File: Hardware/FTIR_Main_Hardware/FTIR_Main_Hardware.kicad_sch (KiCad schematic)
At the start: 64 parts, among them J1 RJ45_LED_Shielded, Q1 IRF7606PBF, Q2 BSS138, Q3 IRF7606PBF, Q4 IRF7606PBF, Q5 BSS138, Q6 BSS138, U1 MCP6L01x-xOT, U3 OKI, U5 MCP6L01x-xOT, U6 Teensy4.1_DEV-16771, U7 OKI

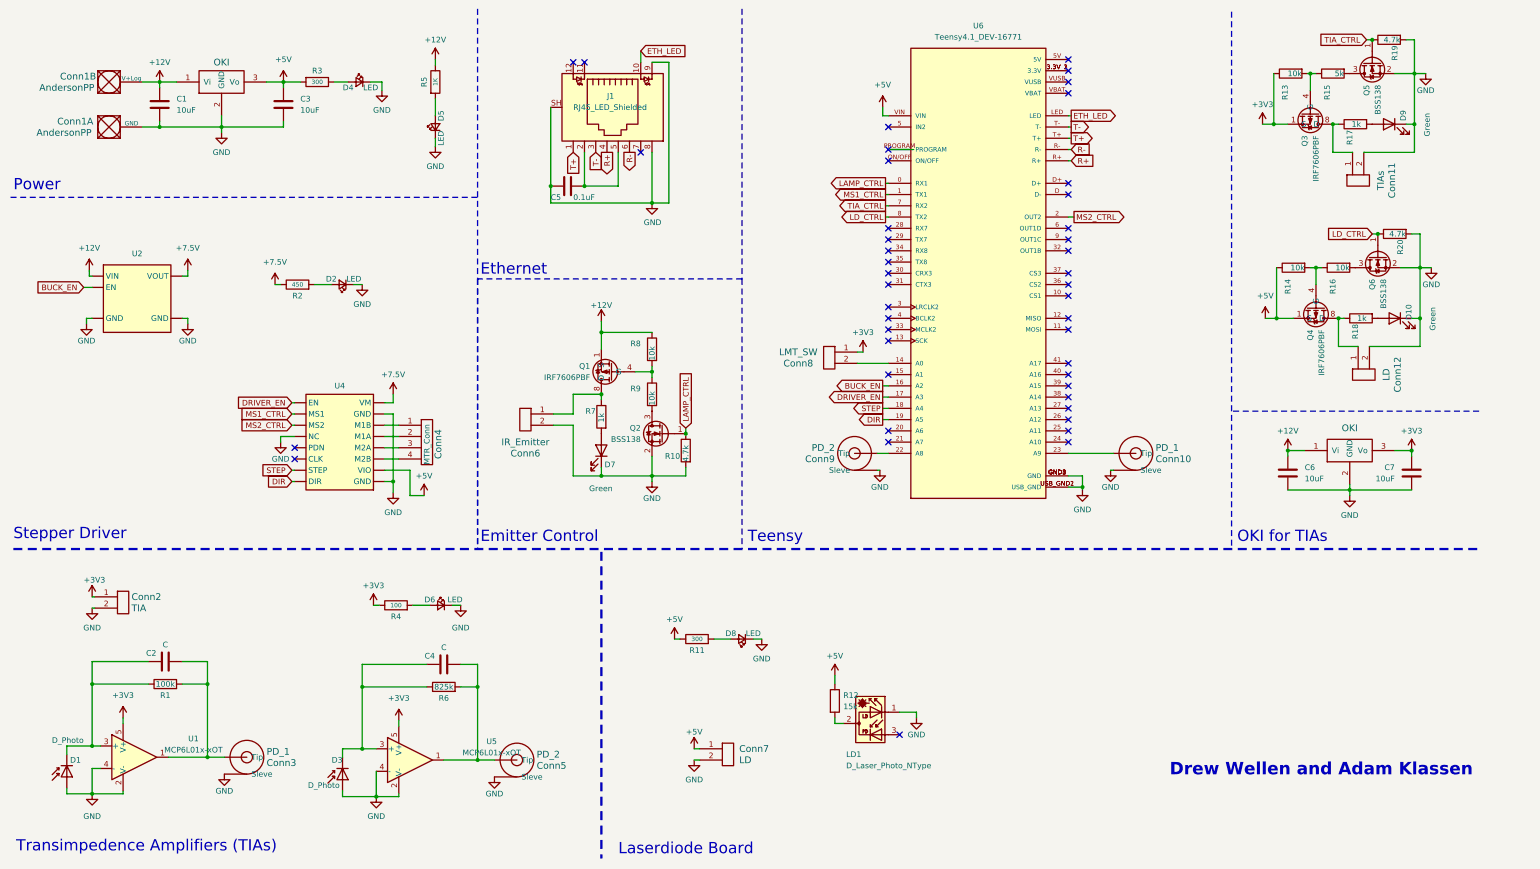
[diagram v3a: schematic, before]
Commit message: changed resistor values
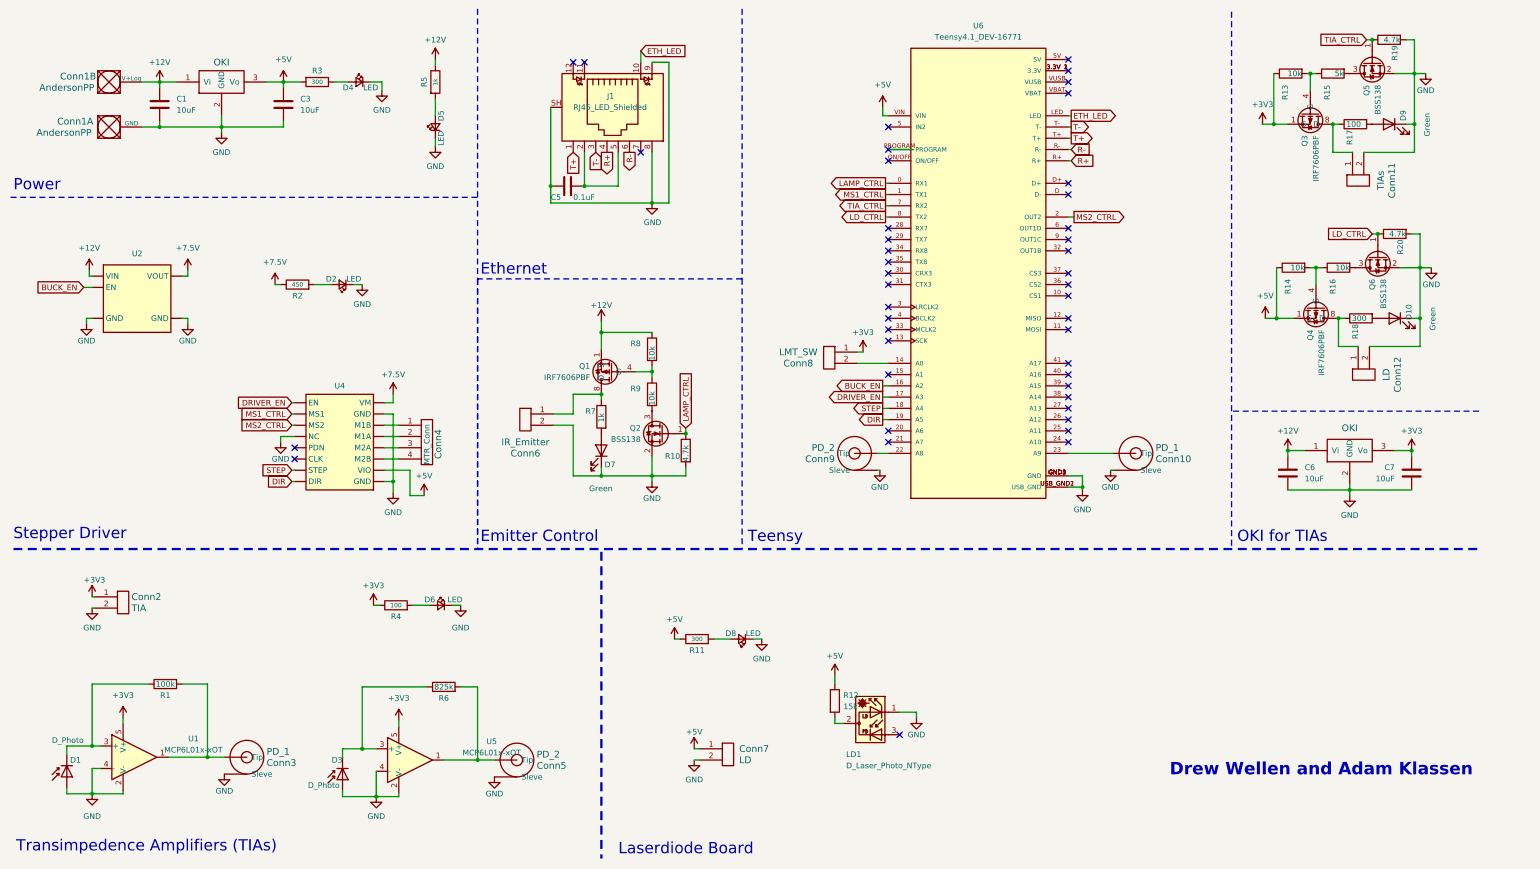
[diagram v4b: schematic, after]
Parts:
- removed C2, C4: C, symbol Device:C
- R17: value 1k -> 100
- R18: value 1k -> 300
- R5: value 1K -> 1k
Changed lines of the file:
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@@
   (junction (at 297.815 81.915) (diameter 0) (color 0 0 0 0)
   )
-  (junction (at 117.475 165.1) (diameter 0) (color 0 0 0 0)
-  )
   (junction (at 328.93 26.67) (diameter 0) (color 0 0 0 0)
   )
@@
   (junction (at 141.605 52.07) (diameter 0) (color 0 0 0 0)
   )
-  (junction (at 30.48 164.465) (diameter 0) (color 0 0 0 0)
-  )
-  (junction (at 56.515 164.465) (diameter 0) (color 0 0 0 0)
-  )
   (junction (at 330.2 70.485) (diameter 0) (color 0 0 0 0)
   )
@@
   (junction (at 91.44 179.07) (diameter 0) (color 0 0 0 0)
   )
-  (junction (at 91.44 165.1) (diameter 0) (color 0 0 0 0)
-  )
   (junction (at 45.72 38.735) (diameter 0) (color 0 0 0 0)
   )
@@
     (stroke (width 0) (type default))
   )
-  (wire (pts (xy 50.8 159.385) (xy 56.515 159.385))
-    (stroke (width 0) (type default))
-  )
   (wire (pts (xy 164.465 117.475) (xy 164.465 115.57))
     (stroke (width 0) (type default))
@@
     (stroke (width 0) (type default))
   )
-  (wire (pts (xy 117.475 160.02) (xy 117.475 165.1))
-    (stroke (width 0) (type default))
-  )
   (wire (pts (xy 319.405 62.865) (xy 320.675 62.865))
     (stroke (width 0) (type default))
@@
     (stroke (width 0) (type default))
   )
-  (wire (pts (xy 56.515 159.385) (xy 56.515 164.465))
-    (stroke (width 0) (type default))
-  )
   (wire (pts (xy 156.845 93.98) (xy 153.035 93.98))
     (stroke (width 0) (type default))
@@
     (stroke (width 0) (type default))
   )
-  (wire (pts (xy 106.045 160.02) (xy 91.44 160.02))
-    (stroke (width 0) (type default))
-  )
   (wire (pts (xy 102.235 116.205) (xy 96.52 116.205))
     (stroke (width 0) (type default))
@@
     (stroke (width 0) (type default))
   )
-  (wire (pts (xy 30.48 159.385) (xy 30.48 164.465))
-    (stroke (width 0) (type default))
-  )
   (wire (pts (xy 328.93 38.1) (xy 327.025 38.1))
     (stroke (width 0) (type default))
@@
     (stroke (width 0) (type dash))
   )
-  (wire (pts (xy 43.18 159.385) (xy 30.48 159.385))
-    (stroke (width 0) (type default))
-  )
   (wire (pts (xy 328.93 19.05) (xy 328.93 26.67))
     (stroke (width 0) (type default))
@@
     (stroke (width 0) (type default))
   )
-  (wire (pts (xy 91.44 160.02) (xy 91.44 165.1))
-    (stroke (width 0) (type default))
-  )
   (wire (pts (xy 76.2 108.585) (xy 73.025 108.585))
     (stroke (width 0) (type default))
@@
     (stroke (width 0) (type default))
   )
-  (wire (pts (xy 113.665 160.02) (xy 117.475 160.02))
-    (stroke (width 0) (type default))
-  )
   (wire (pts (xy 30.48 189.23) (xy 30.48 183.515))
     (stroke (width 0) (type default))
@@
       (effects (font (size 1.27 1.27)))
     )
-    (property "Value" "1K" (at 107.95 28.575 90)
+    (property "Value" "1k" (at 107.95 28.575 90)
       (effects (font (size 0.9906 0.9906)))
     )
@@
       (effects (font (size 1.27 1.27)) (justify left))
     )
-    (property "Value" "1k" (at 316.865 38.1 90)
+    (property "Value" "100" (at 316.865 38.1 90)
       (effects (font (size 1.27 1.27)) (justify left))
     )
@@
     )
   )
-  (symbol (lib_id "Device:C") (at 46.99 159.385 90) (unit 1)
-    (in_bom yes) (on_board yes) (dnp no)
-    (property "Reference" "C2" (at 43.815 157.48 90)
-      (effects (font (size 1.27 1.27)))
-    )
-    (property "Value" "C" (at 46.99 155.575 90)
-      (effects (font (size 1.27 1.27)))
-    )
-    (property "Footprint" "" (at 50.8 158.4198 0)
-      (effects (font (size 1.27 1.27)) hide)
-    )
-    (property "Datasheet" "~" (at 46.99 159.385 0)
-      (effects (font (size 1.27 1.27)) hide)
-    )
-    (pin "1")
-    (pin "2")
-    (instances
-      (project "FTIR_Main_Hardware"
-        (path "/049c3f09-c046-40c3-9872-e62b40667976"
-          (reference "C2") (unit 1)
-        )
-      )
-    )
-  )
   (symbol (lib_id "Device:R") (at 164.465 111.76 0) (mirror y) (unit 1)
     (in_bom yes) (on_board yes) (dnp no)
@@
       (effects (font (size 1.27 1.27)) (justify left))
     )
-    (property "Value" "1k" (at 318.135 81.915 90)
+    (property "Value" "300" (at 318.135 81.915 90)
       (effects (font (size 1.27 1.27)) (justify left))
     )
@@
         )
       )
-    )
-  )
-  (symbol (lib_id "Device:C") (at 109.855 160.02 90) (unit 1)
-    (in_bom yes) (on_board yes) (dnp no)
-    (property "Reference" "C4" (at 106.68 158.115 90)
-      (effects (font (size 1.27 1.27)))
-    )
-    (property "Value" "C" (at 109.855 156.21 90)
-      (effects (font (size 1.27 1.27)))
-    )
-    (property "Footprint" "" (at 113.665 159.0548 0)
-      (effects (font (size 1.27 1.27)) hide)
-    )
-    (property "Datasheet" "~" (at 109.855 160.02 0)
-      (effects (font (size 1.27 1.27)) hide)
-    )
-    (pin "1")
-    (pin "2")
-    (instances
-      (project "FTIR_Main_Hardware"
-        (path "/049c3f09-c046-40c3-9872-e62b40667976"
-          (reference "C4") (unit 1)
-        )
-      )

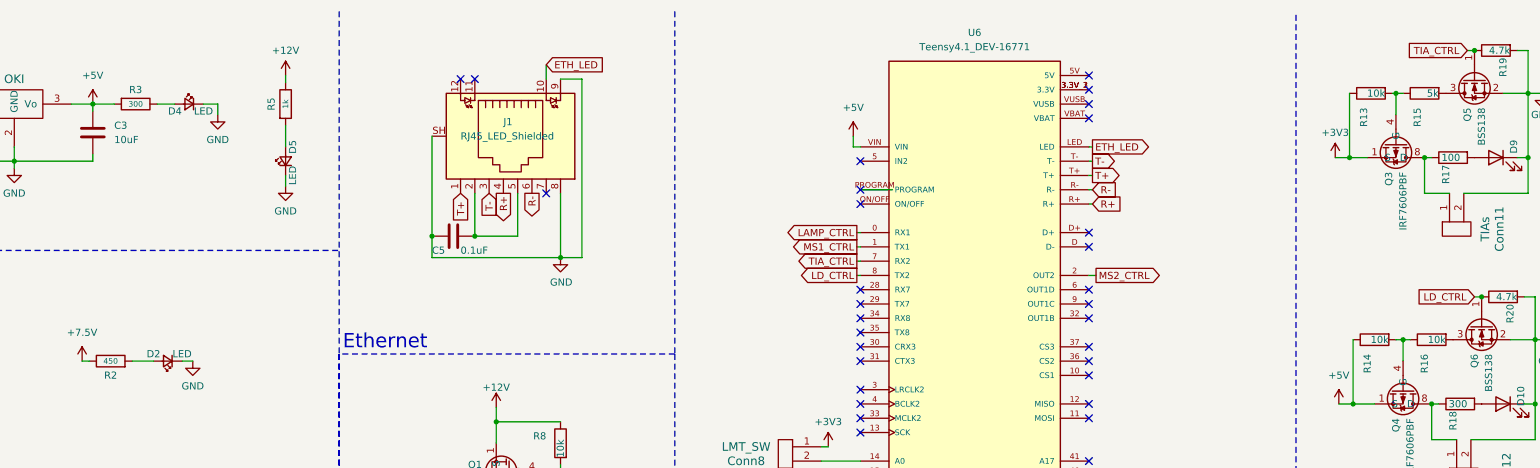
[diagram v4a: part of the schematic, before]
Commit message: Changed capacitor on OKI
Was only rated for 10V but needed 12V. We should change the standard sheet so more people don't burn out their OKIs.
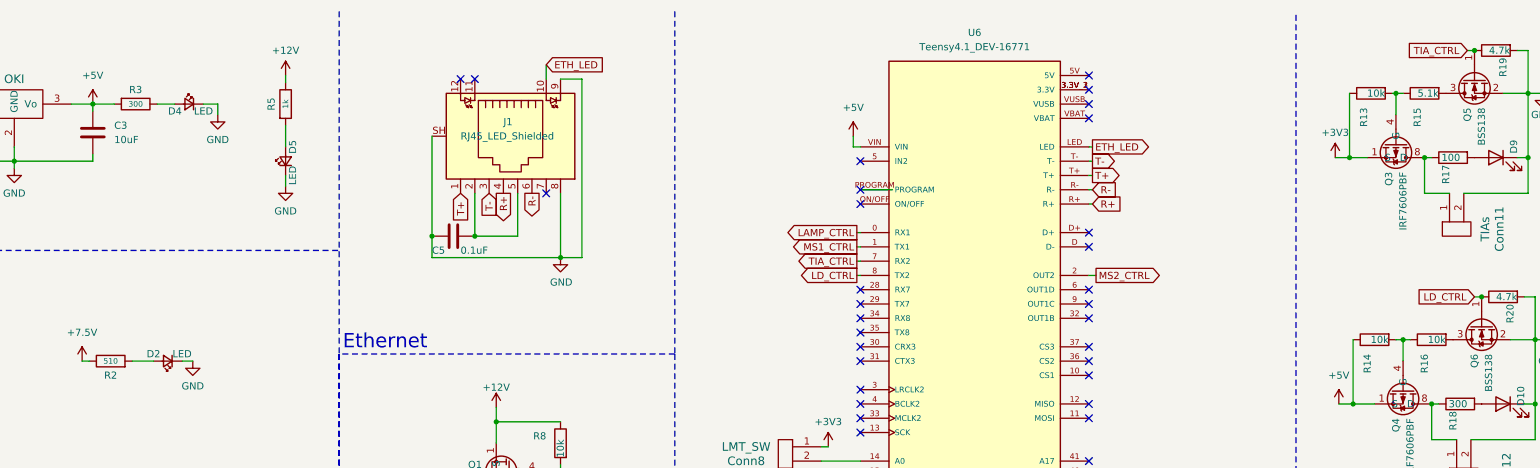
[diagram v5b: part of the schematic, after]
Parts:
- R15: value 5k -> 5.1k
- R2: value 450 -> 510
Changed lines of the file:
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@@
       (effects (font (size 1.27 1.27)))
     )
-    (property "Value" "450" (at 76.835 74.295 90)
+    (property "Value" "510" (at 76.835 74.295 90)
       (effects (font (size 0.9906 0.9906)))
     )
@@
       (effects (font (size 1.27 1.27)) (justify left))
     )
-    (property "Value" "5k" (at 313.055 26.67 90)
-      (effects (font (size 1.27 1.27)) (justify left))
-    )
+    (property "Value" "5.1k" (at 313.055 26.67 90)
+      (effects (font (size 1.27 1.27)) (justify left))
+    )
